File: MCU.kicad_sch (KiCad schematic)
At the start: 40 parts, among them J5 Dupont Debug Headers, SW1 SW_Push, SW2 SW_Push, U1 W25Q128JVS, U2 RP2350_60QFN, Y1 ABM8_262_T3

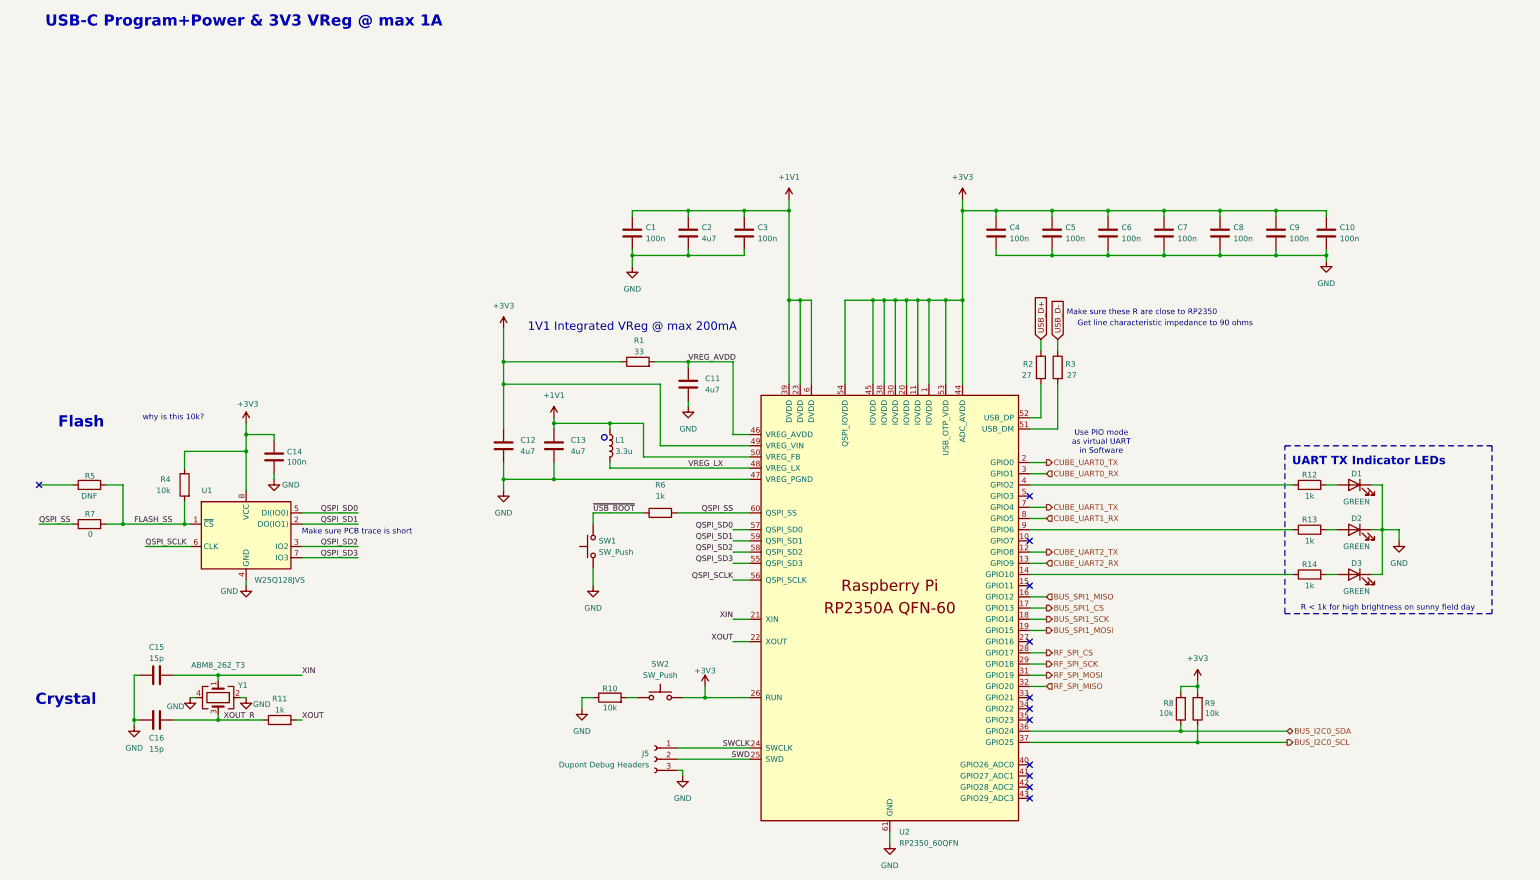
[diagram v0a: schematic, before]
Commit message: Added footprints & routing 30%
- Added Dupont debug headers for UARTs.
- Added footprints: 18650 battery, E32-400M30S.
- Remove Battery Charger due to reliability issue.
- Routing 5V SMPS, 3V3 Regulator, Battery Holder.
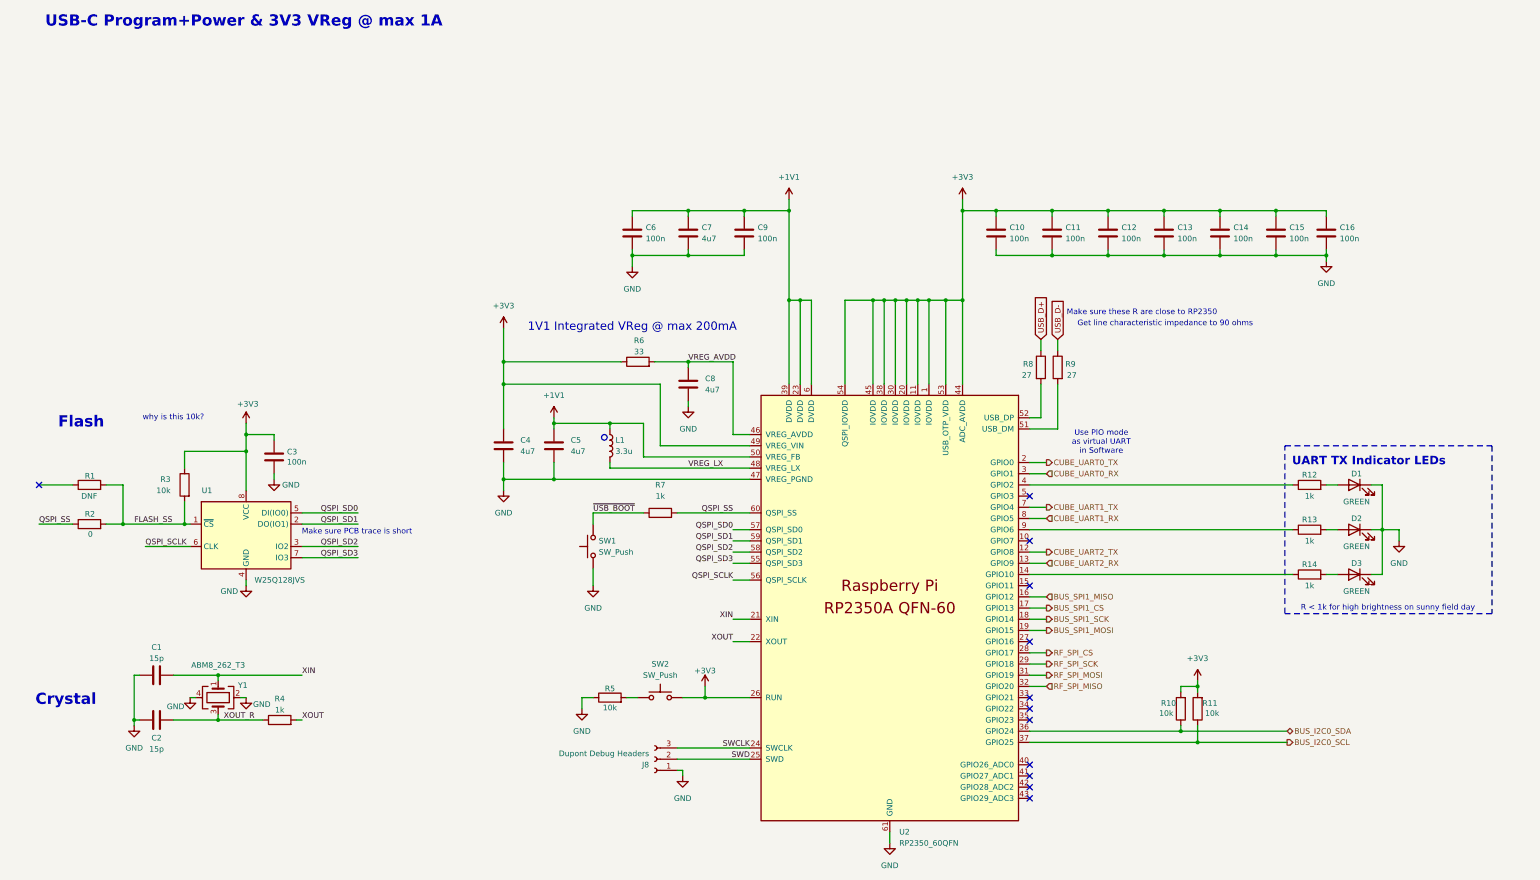
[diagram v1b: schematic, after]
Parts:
- C12: renamed from C6; footprint Capacitor_SMD:C_0402_1005Metric -> Capacitor_SMD:C_0603_1608Metric
- C13: renamed from C7; footprint Capacitor_SMD:C_0402_1005Metric -> Capacitor_SMD:C_0603_1608Metric
- renumbered C15 to C1, C4 to C10, C5 to C11, C8 to C14, C9 to C15, C10 to C16, C16 to C2, C14 to C3, C12 to C4, C13 to C5, C1 to C6, C2 to C7, C11 to C8, C3 to C9, J5 to J8, R5 to R1, R8 to R10, R9 to R11, R7 to R2, R4 to R3, R11 to R4, R10 to R5, R1 to R6, R6 to R7, R2 to R8, R3 to R9
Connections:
- net GND: now also J8.1 (Pin_1); no longer J8.3 (Pin_3)
- net SWCLK: now also J8.3 (Pin_3); no longer J8.1 (Pin_1)
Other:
- moved on the sheet: J8

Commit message: Finished layout & DRC
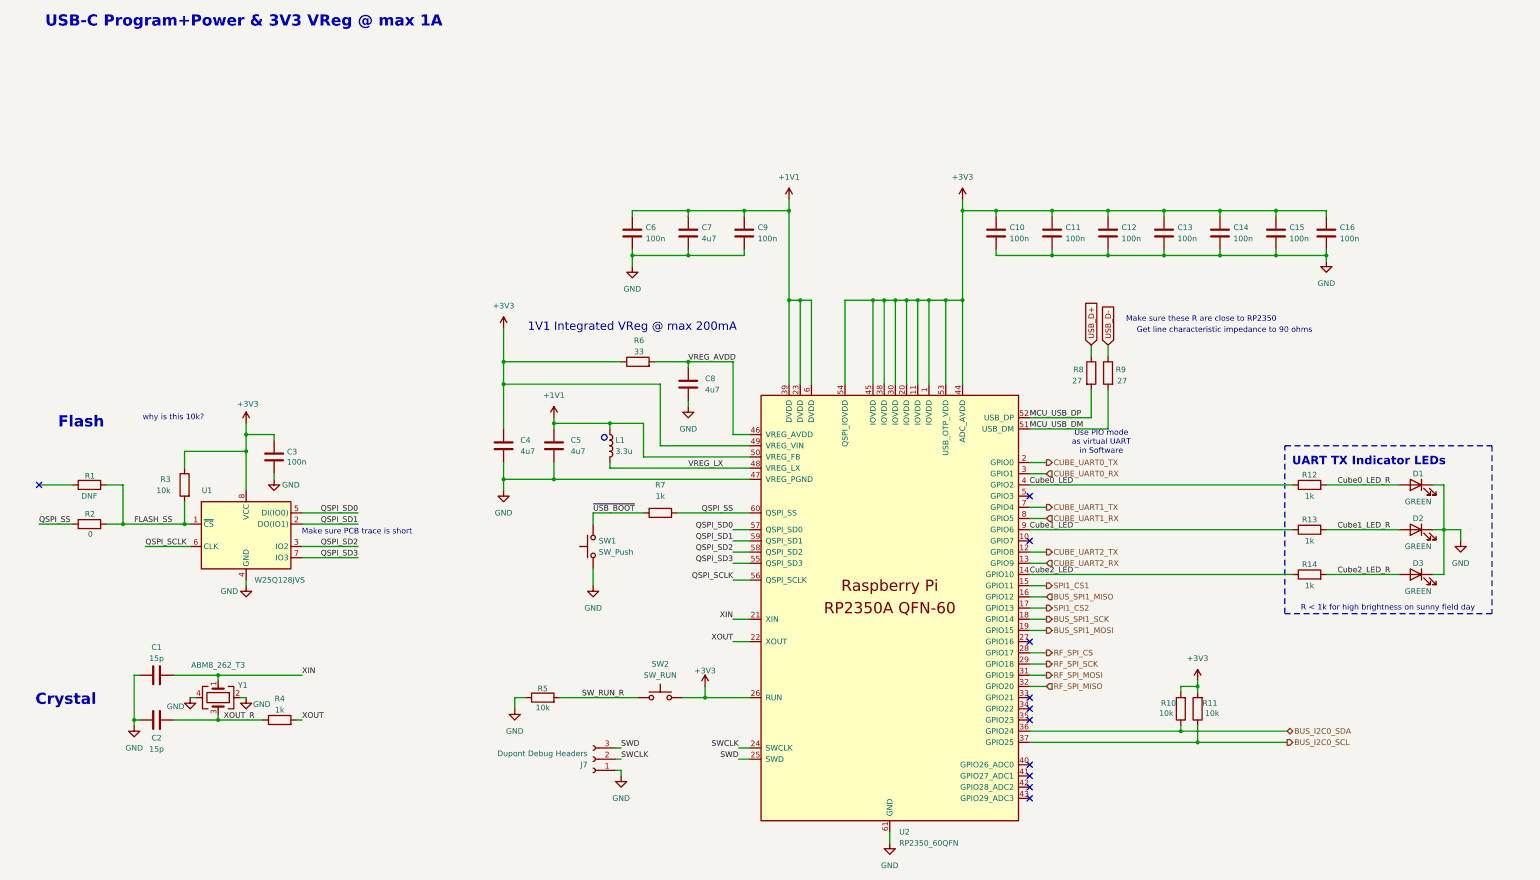
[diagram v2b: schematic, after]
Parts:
- C12, C13, C7: footprint Capacitor_SMD:C_0603_1608Metric -> Capacitor_SMD:C_0402_1005Metric
- R12, R13, R14: footprint Resistor_SMD:R_0805_2012Metric -> Resistor_SMD:R_0603_1608Metric
- R7: footprint Resistor_SMD:R_0603_1608Metric -> Resistor_SMD:R_0402_1005Metric
- SW2: value SW_Push -> SW_RUN
- U2: footprint Package_DFN_QFN:QFN-60-1EP_7x7mm_P0.4mm_EP3.4x3.4mm_ThermalVias -> RP2350_60QFN_minimal:RP2350-QFN-60-1EP_7x7_P0.4mm_EP3.4x3.4mm_ThermalVias
- renumbered J8 to J7
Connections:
- net SWCLK: now also J7.2 (Pin_2); no longer J7.3 (Pin_3)
- net SWD: now also J7.3 (Pin_3); no longer J7.2 (Pin_2)
- net Cube1_LED: now reaches R13.1, U2.9 (GPIO6)
- net Cube1_LED_R: now reaches D2.2 (A), R13.2
- net MCU_USB_DP: now reaches R8.2, U2.52 (USB_DP)
- net Cube2_LED: now reaches R14.1, U2.14 (GPIO10)
- net SPI1_CS1: now reaches U2.15 (GPIO11)
- net Cube0_LED: now reaches R12.1, U2.4 (GPIO2)
- net MCU_USB_DM: now reaches R9.2, U2.51 (USB_DM)
- net Cube2_LED_R: now reaches D3.2 (A), R14.2
- net Cube0_LED_R: now reaches D1.2 (A), R12.2
- net SW_RUN_R: now reaches R5.2, SW2.1
- net BUS_SPI1_CS renamed SPI1_CS2
- no-connect marks 12 -> 11
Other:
- moved on the sheet: D1, D2, D3, J7, R5, R8, R9

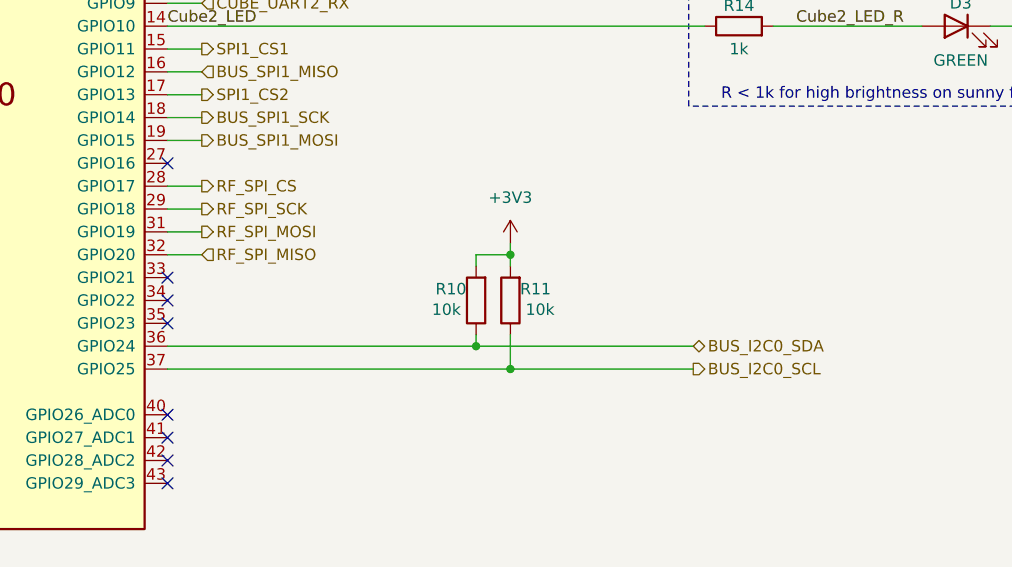
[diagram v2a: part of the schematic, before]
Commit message: Updated EBYTE placement
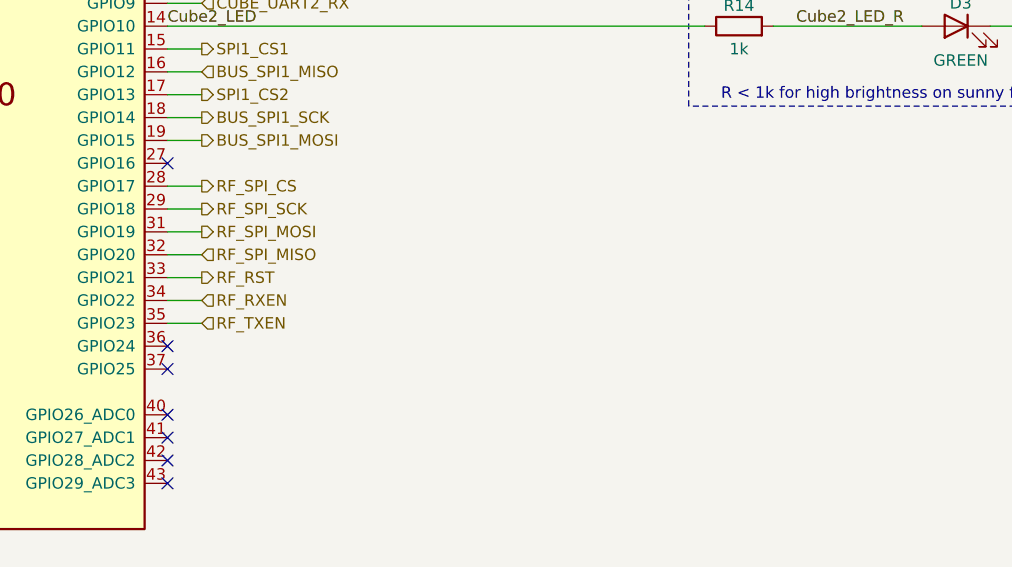
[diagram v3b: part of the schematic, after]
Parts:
- removed R10, R11: 10k, Resistor_SMD:R_0402_1005Metric, symbol Device:R
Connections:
- net RF_RST: now reaches U2.33 (GPIO21)
- net RF_RXEN: now reaches U2.34 (GPIO22)
- net RF_TXEN: now reaches U2.35 (GPIO23)
- net BUS_I2C0_SCL: no longer names the net of U2.37 (GPIO25)
- net BUS_I2C0_SDA: no longer names the net of U2.36 (GPIO24)
- no-connect marks 11 -> 10

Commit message: Added silkscreens label description and fixed DRC
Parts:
- U2: footprint RP2350_60QFN_minimal:RP2350-QFN-60-1EP_7x7_P0.4mm_EP3.4x3.4mm_ThermalVias -> Package_DFN_QFN:QFN-60-1EP_7x7mm_P0.4mm_EP3.4x3.4mm
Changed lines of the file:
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@@
 			)
 		)
-		(property "Footprint" "RP2350_60QFN_minimal:RP2350-QFN-60-1EP_7x7_P0.4mm_EP3.4x3.4mm_ThermalVias"
+		(property "Footprint" "Package_DFN_QFN:QFN-60-1EP_7x7mm_P0.4mm_EP3.4x3.4mm"
 			(at 193.04 149.86 0)
 			(effects

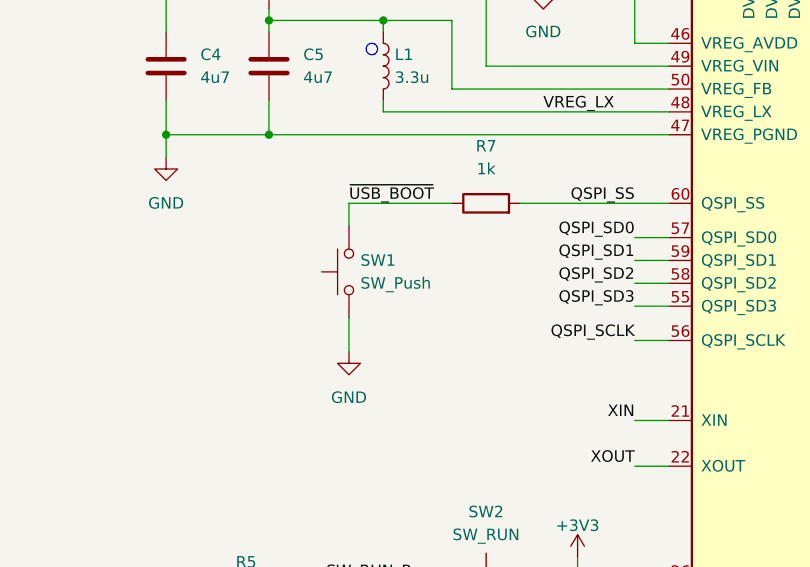
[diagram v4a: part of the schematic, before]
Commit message: Added 3D models and LCSC part numbers
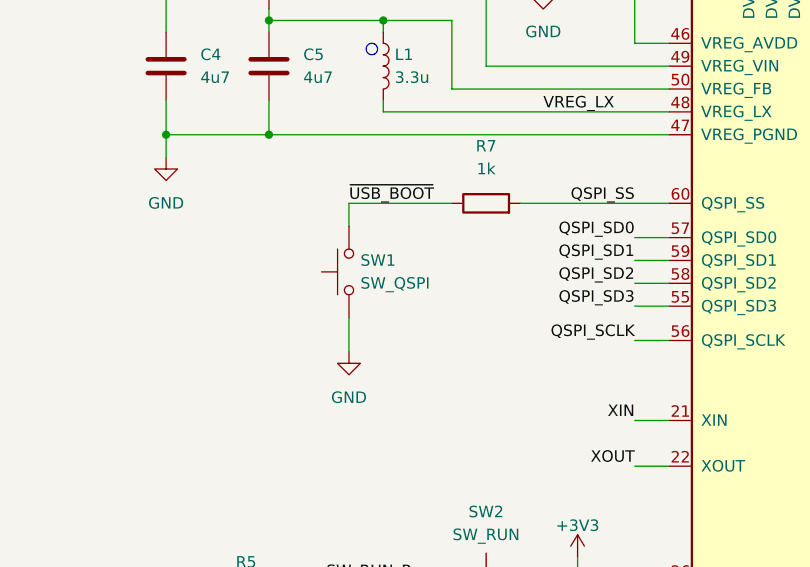
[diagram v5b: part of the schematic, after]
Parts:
- L1: LCSC Part (none) -> C42411119
- SW1: value SW_Push -> SW_QSPI
- U1: LCSC Part (none) -> C97521
- U2: LCSC Part (none) -> C42411118
- Y1: LCSC Part (none) -> C20625731

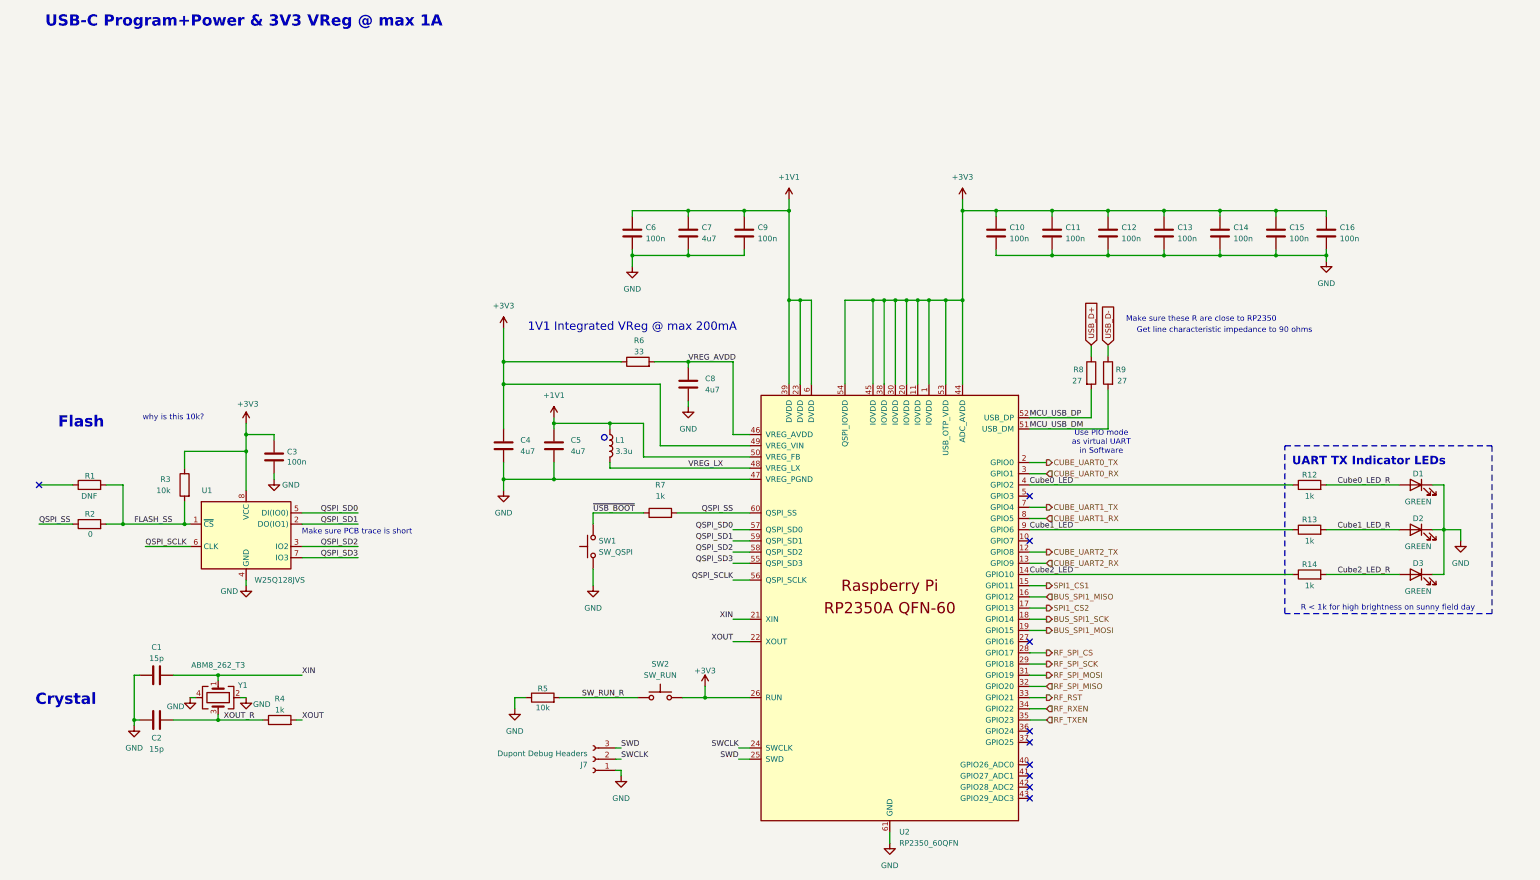
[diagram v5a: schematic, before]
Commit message: General DFM fixes
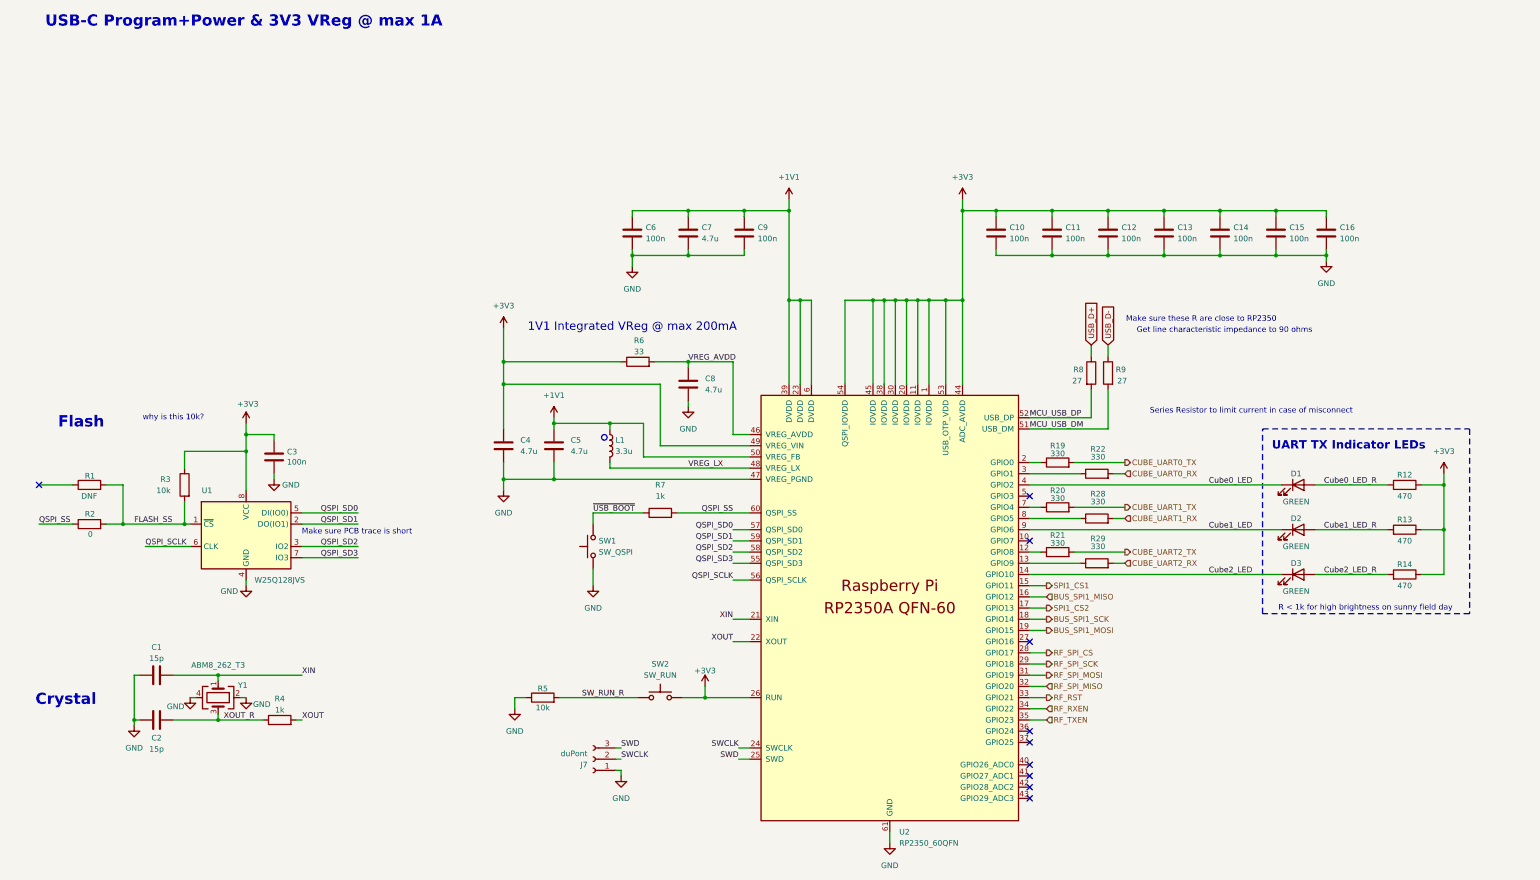
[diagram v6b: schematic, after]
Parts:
- added R19, R20, R21, R22, R28, R29: 330, Resistor_SMD:R_0402_1005Metric, symbol Device:R
- C1, C2: LCSC Part (none) -> C86285
- C10, C11, C12, C13, C14, C15, C16, C3, C6, C9: LCSC Part (none) -> C1525
- C4, C5: value 4u7 -> 4.7u
- C7, C8: value 4u7 -> 4.7u; LCSC Part (none) -> C23733
- J7: value Dupont Debug Headers -> duPont
- R12, R13, R14: value 1k -> 470
- SW1, SW2: LCSC Part (none) -> C720477
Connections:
- net +3V3: now also R12.1, R13.1, R14.1
- net CUBE_UART0_RX: now also R22.2; no longer U2.3 (GPIO1)
- net CUBE_UART0_TX: now also R19.2; no longer U2.2 (GPIO0)
- net CUBE_UART1_RX: now also R28.2; no longer U2.8 (GPIO5)
- net CUBE_UART1_TX: now also R20.2; no longer U2.7 (GPIO4)
- net CUBE_UART2_RX: now also R29.2; no longer U2.13 (GPIO9)
- net CUBE_UART2_TX: now also R21.2; no longer U2.12 (GPIO8)
- net Cube0_LED: now also D1.1 (K); no longer R12.1
- net Cube1_LED: now also D2.1 (K); no longer R13.1
- net Cube2_LED: now also D3.1 (K); no longer R14.1
- net GND: no longer D1.1 (K), D2.1 (K), D3.1 (K)
- new net: R29.1, U2.13 (GPIO9)
- new net: R21.1, U2.12 (GPIO8)
- new net: R19.1, U2.2 (GPIO0)
- new net: R22.1, U2.3 (GPIO1)
- new net: R20.1, U2.7 (GPIO4)
- new net: R28.1, U2.8 (GPIO5)
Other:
- note added: "Series Resistor to limit current in case of misconnect"
- note removed: "Use PIO mode as virtual UART in Software"
- moved on the sheet: D1, D2, D3, R12, R13, R14
